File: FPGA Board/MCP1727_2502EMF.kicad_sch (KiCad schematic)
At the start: 16 parts, among them U3 MCP1727-2502xMF

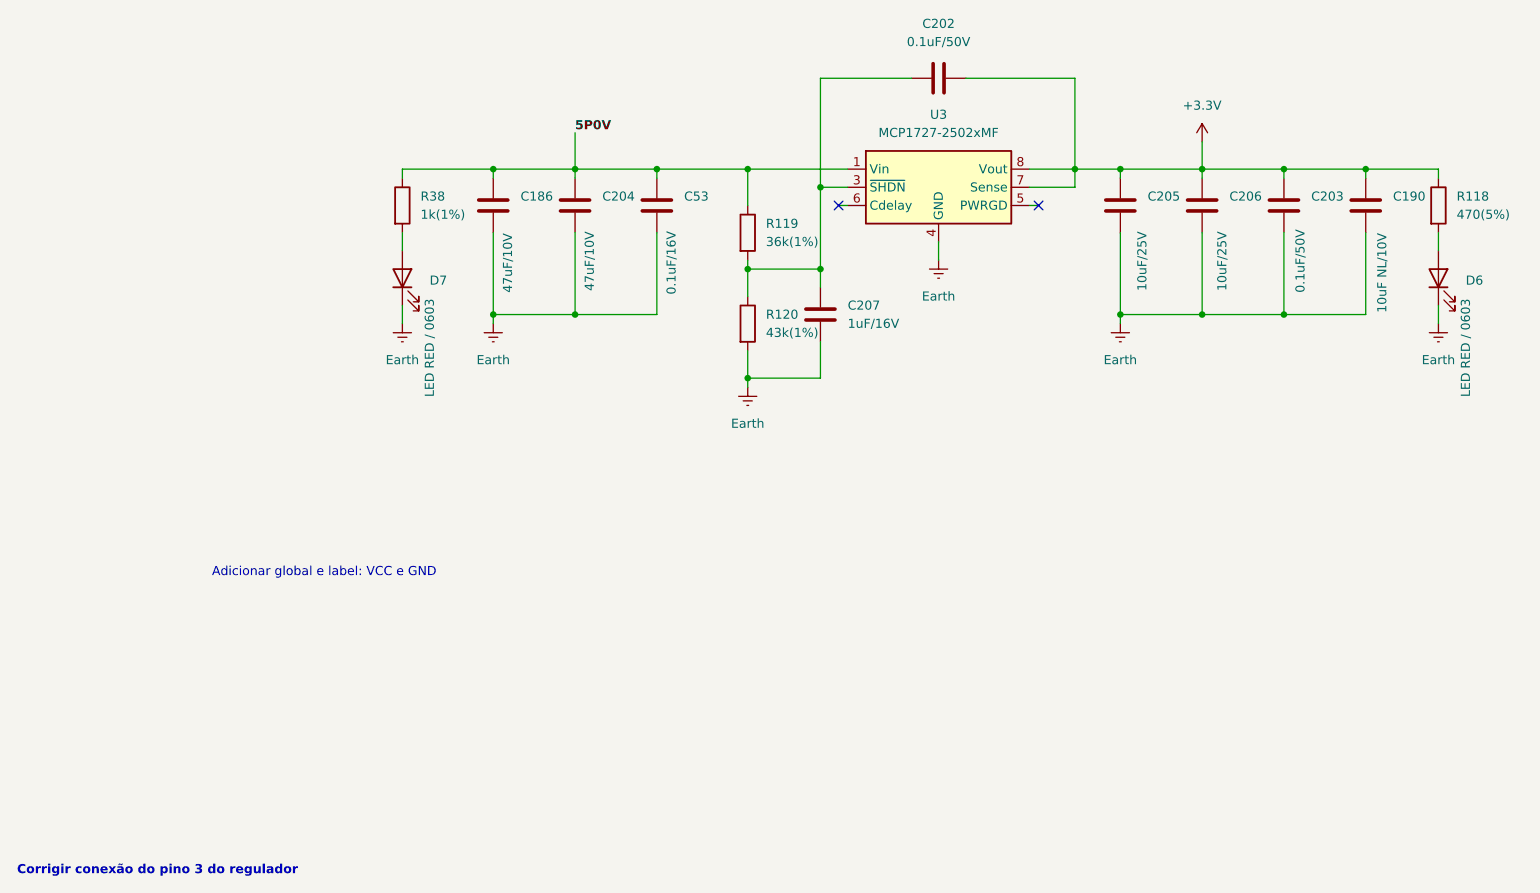
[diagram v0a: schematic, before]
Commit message: Inclusão do projeto KiCad, datasheets, símbolos, footprints, modelos 3D, correções de etiquetas hierarquicas e globais.
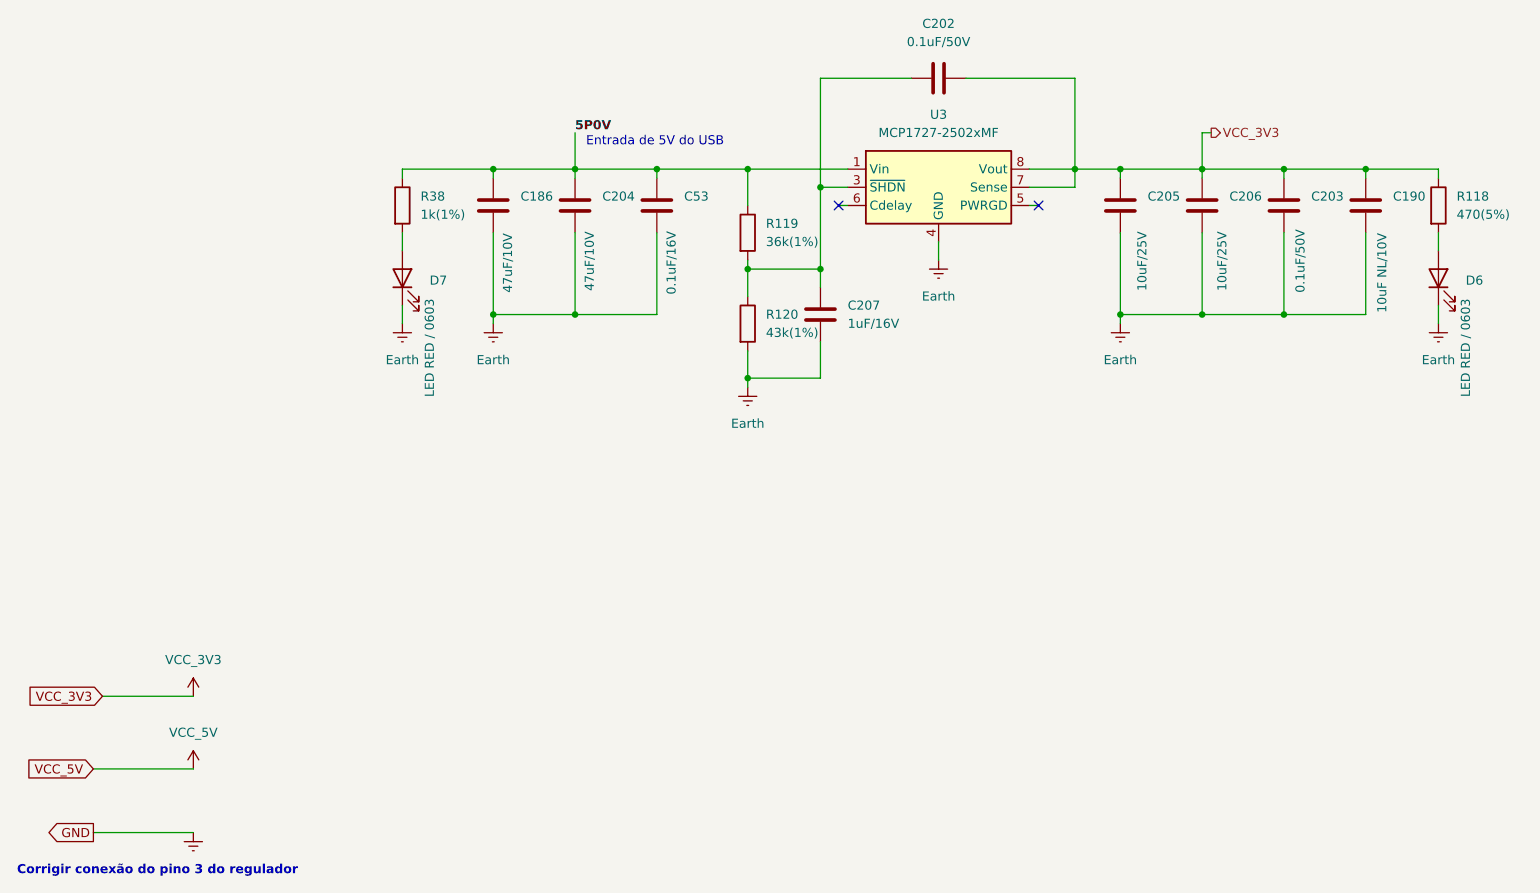
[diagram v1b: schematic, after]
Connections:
- net +3.3V renamed VCC_3V3
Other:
- note added: "Entrada de 5V do USB"
- note removed: "Adicionar global e label: VCC e GND"
